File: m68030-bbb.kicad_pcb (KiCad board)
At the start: 2 copper layers, 6 parts, among them U1 MC68030, U2 XC95108TQ100, U3 IS61C25616AL, U4 M29F400F, U5 IS61C25616AL, U6 M29F400F

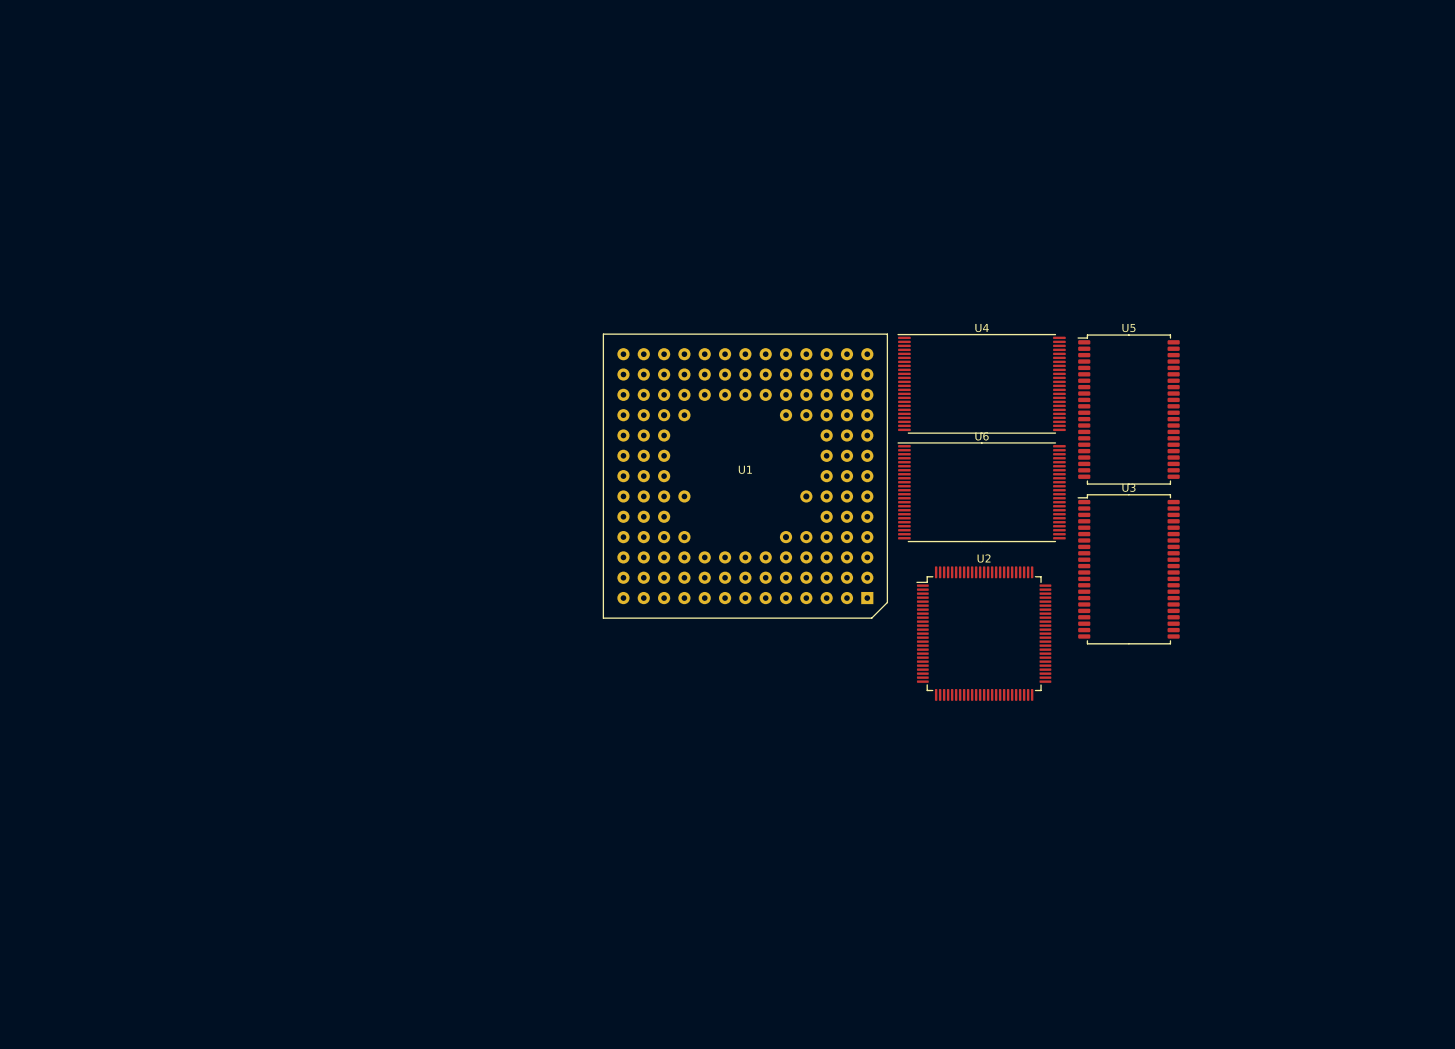
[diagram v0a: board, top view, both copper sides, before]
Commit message: Add MPCC and PIT, move things around.  Still need to decide on CPLD to use.
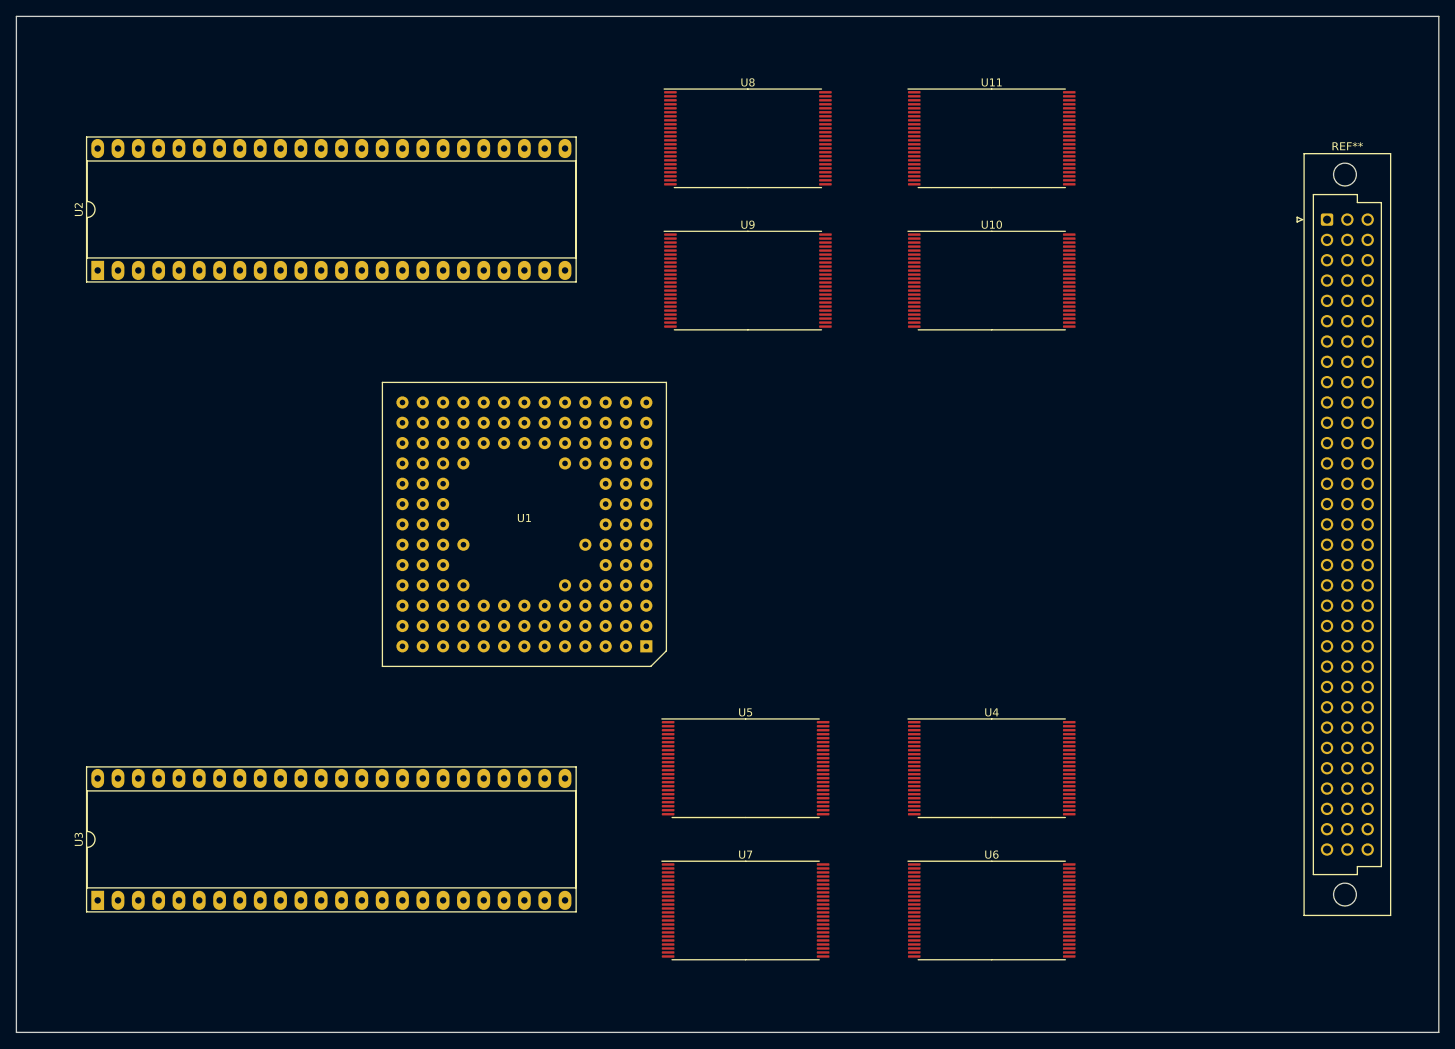
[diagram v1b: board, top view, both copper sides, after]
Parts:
- added REF**: DIN41612_C_3x32_Female_Vertical_THT, Connector_DIN:DIN41612_C_3x32_Female_Vertical_THT, F.Cu at (252.7, 44.5)
- added U10: M29F160F, Package_SO:TSOP-I-48_18.4x12mm_P0.5mm, F.Cu at (210.8, 52.1)
- added U11: M29F160F, Package_SO:TSOP-I-48_18.4x12mm_P0.5mm, F.Cu at (210.8, 34.3)
- added U7: CY62167GN-45ZXI, Package_SO:TSOP-I-48_18.4x12mm_P0.5mm, F.Cu at (180.1, 130.8)
- added U8: M29F160F, Package_SO:TSOP-I-48_18.4x12mm_P0.5mm, F.Cu at (180.3, 34.3)
- added U9: M29F160F, Package_SO:TSOP-I-48_18.4x12mm_P0.5mm, F.Cu at (180.3, 52.1)
- U2: value XC95108TQ100 -> R68561; footprint Package_QFP:TQFP-100_14x14mm_P0.5mm -> Package_DIP:DIP-48_W15.24mm_Socket_LongPads
- U3: value IS61C25616AL -> 68230; footprint Package_SO:TSOP-II-44_10.16x18.41mm_P0.8mm -> Package_DIP:DIP-48_W15.24mm_Socket_LongPads
- U4, U6: value M29F400F -> CY62167GN-45ZXI
- U5: value IS61C25616AL -> CY62167GN-45ZXI; footprint Package_SO:TSOP-II-44_10.16x18.41mm_P0.8mm -> Package_SO:TSOP-I-48_18.4x12mm_P0.5mm
- moved U3 135.4 mm to (99.1, 129.5), turned to 90 degrees
- moved U2 119.7 mm to (99.1, 50.8), turned to 90 degrees
- moved U5 65.6 mm to (180.1, 113.0)
- moved U6 52.3 mm to (210.8, 130.8)
- moved U4 48.1 mm to (210.8, 113.0)
- moved U1 28.3 mm to (152.4, 82.5)
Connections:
- U1 pad A1: unconnected-(U1-PadA1) -> /~{BR}
- U1 pad A10: unconnected-(U1-PadA10) -> /A17
- U1 pad A11: unconnected-(U1-PadA11) -> /A15
- U1 pad A12: unconnected-(U1-PadA12) -> /A13
- U1 pad A13: unconnected-(U1-PadA13) -> /A10
- U1 pad A2: unconnected-(U1-PadA2) -> /A0
- U1 pad A3: unconnected-(U1-PadA3) -> /A30
- U1 pad A4: unconnected-(U1-PadA4) -> /A28
- U1 pad A5: unconnected-(U1-PadA5) -> /A26
- U1 pad A6: unconnected-(U1-PadA6) -> /A24
- U1 pad A7: unconnected-(U1-PadA7) -> /A23
- U1 pad A8: unconnected-(U1-PadA8) -> /A21
- U1 pad A9: unconnected-(U1-PadA9) -> /A19
- U1 pad B1: unconnected-(U1-PadB1) -> /~{RMC}
- U1 pad B10: unconnected-(U1-PadB10) -> /A14
- U1 pad B11: unconnected-(U1-PadB11) -> /A12
- U1 pad B12: unconnected-(U1-PadB12) -> /A8
- U1 pad B13: unconnected-(U1-PadB13) -> /A7
- U1 pad B2: unconnected-(U1-PadB2) -> /~{BG}
- U1 pad B3: unconnected-(U1-PadB3) -> /A31
- U1 pad B4: unconnected-(U1-PadB4) -> /A29
- U1 pad B5: unconnected-(U1-PadB5) -> /A27
- U1 pad B6: unconnected-(U1-PadB6) -> /A25
- U1 pad B7: unconnected-(U1-PadB7) -> /A22
- U1 pad B8: unconnected-(U1-PadB8) -> /A20
- U1 pad B9: unconnected-(U1-PadB9) -> /A16
- U1 pad C1: unconnected-(U1-PadC1) -> /FC1
- U1 pad C10: unconnected-(U1-PadC10) -> /A11
- U1 pad C11: unconnected-(U1-PadC11) -> /A9
- U1 pad C12: unconnected-(U1-PadC12) -> /A5
- U1 pad C13: unconnected-(U1-PadC13) -> /A4
- U1 pad C3: unconnected-(U1-PadC3) -> /~{BGACK}
- U1 pad C4: unconnected-(U1-PadC4) -> /A1
- U1 pad C5: unconnected-(U1-PadC5) -> GND
- U1 pad C6: unconnected-(U1-PadC6) -> +5V
- U1 pad C7: unconnected-(U1-PadC7) -> GND
- U1 pad C8: unconnected-(U1-PadC8) -> /A18
- U1 pad C9: unconnected-(U1-PadC9) -> GND
- U1 pad D1: unconnected-(U1-PadD1) -> /FC2
- U1 pad D10: unconnected-(U1-PadD10) -> +5V
- U1 pad D11: unconnected-(U1-PadD11) -> /A6
- U1 pad D12: unconnected-(U1-PadD12) -> /A3
- U1 pad D13: unconnected-(U1-PadD13) -> /A2
- U1 pad D2: unconnected-(U1-PadD2) -> /FC0
- U1 pad D3: unconnected-(U1-PadD3) -> /~{OCS}
- U1 pad D4: unconnected-(U1-PadD4) -> +5V
- U1 pad E1: unconnected-(U1-PadE1) -> /CLK
- U1 pad E11: unconnected-(U1-PadE11) -> GND
- U1 pad E13: unconnected-(U1-PadE13) -> /~{IPEND}
- U1 pad E2: unconnected-(U1-PadE2) -> /~{AVEC}
- U1 pad E3: unconnected-(U1-PadE3) -> GND
- U1 pad F1: unconnected-(U1-PadF1) -> /~{DSACK0}
- U1 pad F11: unconnected-(U1-PadF11) -> +5V
- U1 pad F12: unconnected-(U1-PadF12) -> /~{RESET}
- U1 pad F2: unconnected-(U1-PadF2) -> +5V
- U1 pad F3: unconnected-(U1-PadF3) -> GND
- U1 pad G1: unconnected-(U1-PadG1) -> /~{STERM}
- U1 pad G11: unconnected-(U1-PadG11) -> GND
- U1 pad G12: unconnected-(U1-PadG12) -> /~{IPL2}
- U1 pad G13: unconnected-(U1-PadG13) -> /~{IPL1}
- U1 pad G2: unconnected-(U1-PadG2) -> /~{DSACK1}
- U1 pad G3: unconnected-(U1-PadG3) -> GND
- U1 pad H1: unconnected-(U1-PadH1) -> /~{BERR}
- U1 pad H11: unconnected-(U1-PadH11) -> +5V
- U1 pad H13: unconnected-(U1-PadH13) -> /~{IPL0}
- U1 pad H2: unconnected-(U1-PadH2) -> /~{HALT}
- U1 pad H3: unconnected-(U1-PadH3) -> +5V
- U1 pad J11: unconnected-(U1-PadJ11) -> GND
- U1 pad J2: unconnected-(U1-PadJ2) -> /~{AS}
- U1 pad J3: unconnected-(U1-PadJ3) -> GND
- U1 pad K10: unconnected-(U1-PadK10) -> +5V
- U1 pad K11: unconnected-(U1-PadK11) -> /D5
- U1 pad K12: unconnected-(U1-PadK12) -> /D1
- U1 pad K13: unconnected-(U1-PadK13) -> /D0
- U1 pad K2: unconnected-(U1-PadK2) -> /~{DS}
- U1 pad K4: unconnected-(U1-PadK4) -> +5V
- U1 pad L10: unconnected-(U1-PadL10) -> /D10
- U1 pad L11: unconnected-(U1-PadL11) -> /D7
- U1 pad L12: unconnected-(U1-PadL12) -> /D4
- U1 pad L13: unconnected-(U1-PadL13) -> /D2
- U1 pad L3: unconnected-(U1-PadL3) -> /R/~{W}
- U1 pad L4: unconnected-(U1-PadL4) -> /D30
- U1 pad L5: unconnected-(U1-PadL5) -> GND
- U1 pad L6: unconnected-(U1-PadL6) -> +5V
- U1 pad L7: unconnected-(U1-PadL7) -> GND
- U1 pad L8: unconnected-(U1-PadL8) -> GND
- U1 pad L9: unconnected-(U1-PadL9) -> GND
- U1 pad M10: unconnected-(U1-PadM10) -> /D12
- U1 pad M11: unconnected-(U1-PadM11) -> /D9
- U1 pad M12: unconnected-(U1-PadM12) -> /D6
- U1 pad M13: unconnected-(U1-PadM13) -> /D3
- U1 pad M2: unconnected-(U1-PadM2) -> /~{ECS}
- U1 pad M3: unconnected-(U1-PadM3) -> /D29
- U1 pad M4: unconnected-(U1-PadM4) -> /D27
- U1 pad M5: unconnected-(U1-PadM5) -> /D24
- U1 pad M6: unconnected-(U1-PadM6) -> /D22
- U1 pad M7: unconnected-(U1-PadM7) -> /D20
- U1 pad M8: unconnected-(U1-PadM8) -> /D17
- U1 pad M9: unconnected-(U1-PadM9) -> /D14
- U1 pad N1: unconnected-(U1-PadN1) -> /D31
- U1 pad N10: unconnected-(U1-PadN10) -> /D15
- U1 pad N11: unconnected-(U1-PadN11) -> /D13
- U1 pad N12: unconnected-(U1-PadN12) -> /D11
- U1 pad N13: unconnected-(U1-PadN13) -> /D8
- U1 pad N2: unconnected-(U1-PadN2) -> /D28
- U1 pad N3: unconnected-(U1-PadN3) -> /D26
- U1 pad N4: unconnected-(U1-PadN4) -> /D25
- U1 pad N5: unconnected-(U1-PadN5) -> /D23
- U1 pad N6: unconnected-(U1-PadN6) -> /D21
- U1 pad N7: unconnected-(U1-PadN7) -> /D19
- U1 pad N8: unconnected-(U1-PadN8) -> /D18
- U1 pad N9: unconnected-(U1-PadN9) -> /D16
- U3 pad 28: (no net) -> unconnected-(U3-Pad28)
- U4 pad 1: unconnected-(U4-Pad1) -> /A17
- U4 pad 11: unconnected-(U4-Pad11) -> /~{WELL}
- U4 pad 12: unconnected-(U4-Pad12) -> Net-(U4-Pad12)
- U4 pad 14: unconnected-(U4-Pad14) -> Net-(U4-Pad12)
- U4 pad 15: unconnected-(U4-Pad15) -> Net-(U4-Pad12)
- U4 pad 16: unconnected-(U4-Pad16) -> /A20
- U4 pad 17: unconnected-(U4-Pad17) -> /A19
- U4 pad 18: unconnected-(U4-Pad18) -> /A9
- U4 pad 19: unconnected-(U4-Pad19) -> /A8
- U4 pad 2: unconnected-(U4-Pad2) -> /A16
- U4 pad 20: unconnected-(U4-Pad20) -> /A7
- U4 pad 21: unconnected-(U4-Pad21) -> /A6
- U4 pad 22: unconnected-(U4-Pad22) -> /A5
- U4 pad 23: unconnected-(U4-Pad23) -> /A4
- U4 pad 24: unconnected-(U4-Pad24) -> /A3
- U4 pad 25: unconnected-(U4-Pad25) -> /A2
- U4 pad 26: unconnected-(U4-Pad26) -> /~{RAMCE}
- U4 pad 27: unconnected-(U4-Pad27) -> GND
- U4 pad 28: unconnected-(U4-Pad28) -> /~{RDLL}
- U4 pad 29: unconnected-(U4-Pad29) -> /D0
- U4 pad 3: unconnected-(U4-Pad3) -> /A15
- U4 pad 31: unconnected-(U4-Pad31) -> /D1
- U4 pad 33: unconnected-(U4-Pad33) -> /D2
- U4 pad 35: unconnected-(U4-Pad35) -> /D3
- U4 pad 38: unconnected-(U4-Pad38) -> /D4
- U4 pad 4: unconnected-(U4-Pad4) -> /A14
- U4 pad 40: unconnected-(U4-Pad40) -> /D5
- U4 pad 42: unconnected-(U4-Pad42) -> /D6
- U4 pad 44: unconnected-(U4-Pad44) -> /D7
- U4 pad 45: unconnected-(U4-Pad45) -> /A22
- U4 pad 46: unconnected-(U4-Pad46) -> GND
- U4 pad 47: unconnected-(U4-Pad47) -> GND
- U4 pad 48: unconnected-(U4-Pad48) -> /A18
- U4 pad 5: unconnected-(U4-Pad5) -> /A13
- U4 pad 6: unconnected-(U4-Pad6) -> /A12
- U4 pad 7: unconnected-(U4-Pad7) -> /A11
- U4 pad 8: unconnected-(U4-Pad8) -> /A10
- U4 pad 9: unconnected-(U4-Pad9) -> /A21
- U5 pad 1: unconnected-(U5-Pad1) -> /A17
- U5 pad 11: unconnected-(U5-Pad11) -> /~{WELM}
- U5 pad 12: unconnected-(U5-Pad12) -> Net-(U5-Pad12)
- U5 pad 14: unconnected-(U5-Pad14) -> Net-(U5-Pad12)
- U5 pad 15: unconnected-(U5-Pad15) -> Net-(U5-Pad12)
- U5 pad 16: unconnected-(U5-Pad16) -> /A20
- U5 pad 17: unconnected-(U5-Pad17) -> /A19
- U5 pad 18: unconnected-(U5-Pad18) -> /A9
- U5 pad 19: unconnected-(U5-Pad19) -> /A8
- U5 pad 2: unconnected-(U5-Pad2) -> /A16
- U5 pad 20: unconnected-(U5-Pad20) -> /A7
- U5 pad 21: unconnected-(U5-Pad21) -> /A6
- U5 pad 22: unconnected-(U5-Pad22) -> /A5
- U5 pad 23: unconnected-(U5-Pad23) -> /A4
- U5 pad 24: unconnected-(U5-Pad24) -> /A3
- U5 pad 25: unconnected-(U5-Pad25) -> /A2
- U5 pad 26: unconnected-(U5-Pad26) -> /~{RAMCE}
- U5 pad 27: unconnected-(U5-Pad27) -> GND
- U5 pad 28: (no net) -> /~{RDLM}
- U5 pad 29: unconnected-(U5-Pad29) -> /D8
- U5 pad 3: unconnected-(U5-Pad3) -> /A15
- U5 pad 31: unconnected-(U5-Pad31) -> /D9
- U5 pad 33: unconnected-(U5-Pad33) -> /D10
- U5 pad 35: unconnected-(U5-Pad35) -> /D11
- U5 pad 38: unconnected-(U5-Pad38) -> /D12
- U5 pad 4: unconnected-(U5-Pad4) -> /A14
- U5 pad 40: unconnected-(U5-Pad40) -> /D13
- U5 pad 42: unconnected-(U5-Pad42) -> /D14
- U5 pad 44: unconnected-(U5-Pad44) -> /D15
- U5 pad 5: unconnected-(U5-Pad5) -> /A13
- U5 pad 6: unconnected-(U5-Pad6) -> /A12
- U5 pad 7: unconnected-(U5-Pad7) -> /A11
- U5 pad 8: unconnected-(U5-Pad8) -> /A10
- U5 pad 9: unconnected-(U5-Pad9) -> /A21
- U6 pad 1: unconnected-(U6-Pad1) -> /A17
- U6 pad 11: unconnected-(U6-Pad11) -> /~{WEUM}
- U6 pad 12: unconnected-(U6-Pad12) -> Net-(U6-Pad12)
- U6 pad 14: unconnected-(U6-Pad14) -> Net-(U6-Pad12)
- U6 pad 15: unconnected-(U6-Pad15) -> Net-(U6-Pad12)
- U6 pad 16: unconnected-(U6-Pad16) -> /A20
- U6 pad 17: unconnected-(U6-Pad17) -> /A19
- U6 pad 18: unconnected-(U6-Pad18) -> /A9
- U6 pad 19: unconnected-(U6-Pad19) -> /A8
- U6 pad 2: unconnected-(U6-Pad2) -> /A16
- U6 pad 20: unconnected-(U6-Pad20) -> /A7
- U6 pad 21: unconnected-(U6-Pad21) -> /A6
- U6 pad 22: unconnected-(U6-Pad22) -> /A5
- U6 pad 23: unconnected-(U6-Pad23) -> /A4
- U6 pad 24: unconnected-(U6-Pad24) -> /A3
- U6 pad 25: unconnected-(U6-Pad25) -> /A2
- U6 pad 26: unconnected-(U6-Pad26) -> /~{RAMCE}
- U6 pad 27: unconnected-(U6-Pad27) -> GND
- U6 pad 28: unconnected-(U6-Pad28) -> /~{RDUM}
- U6 pad 29: unconnected-(U6-Pad29) -> /D16
- U6 pad 3: unconnected-(U6-Pad3) -> /A15
- U6 pad 31: unconnected-(U6-Pad31) -> /D17
- U6 pad 33: unconnected-(U6-Pad33) -> /D18
- U6 pad 35: unconnected-(U6-Pad35) -> /D19
- U6 pad 38: unconnected-(U6-Pad38) -> /D20
- U6 pad 4: unconnected-(U6-Pad4) -> /A14
- U6 pad 40: unconnected-(U6-Pad40) -> /D21
- U6 pad 42: unconnected-(U6-Pad42) -> /D22
- U6 pad 44: unconnected-(U6-Pad44) -> /D23
- U6 pad 45: unconnected-(U6-Pad45) -> /A22
- U6 pad 46: unconnected-(U6-Pad46) -> GND
- U6 pad 47: unconnected-(U6-Pad47) -> GND
- U6 pad 48: unconnected-(U6-Pad48) -> /A18
- U6 pad 5: unconnected-(U6-Pad5) -> /A13
- U6 pad 6: unconnected-(U6-Pad6) -> /A12
- U6 pad 7: unconnected-(U6-Pad7) -> /A11
- U6 pad 8: unconnected-(U6-Pad8) -> /A10
- U6 pad 9: unconnected-(U6-Pad9) -> /A21
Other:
- board outline added: 177.8 x 127 mm
- copper layers 2 -> 4

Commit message: More CPLD changes
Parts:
- removed REF**: DIN41612_C_3x32_Female_Vertical_THT, Connector_DIN:DIN41612_C_3x32_Female_Vertical_THT
- added U12: XC95108TQ100, Package_QFP:TQFP-100_14x14mm_P0.5mm, F.Cu at (115.6, 82.5)
- turned U1 to 180 degrees
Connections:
- U1 pad C2: unconnected-(U1-PadC2) -> /~{CIOUT}
- U1 pad E1: /CLK -> /CPUCLK
- U1 pad J1: unconnected-(U1-PadJ1) -> /~{CBACK}
- U1 pad K1: unconnected-(U1-PadK1) -> /~{CBREQ}
- U1 pad K3: unconnected-(U1-PadK3) -> /~{SIZ1}
- U1 pad L1: unconnected-(U1-PadL1) -> /~{CIIN}
- U1 pad L2: unconnected-(U1-PadL2) -> /~{SIZ0}
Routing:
- net GND: vias 0 -> 3
- net +5V: vias 0 -> 3
- added copper zone on In1.Cu, net +5V
- added copper zone on In2.Cu, net GND
